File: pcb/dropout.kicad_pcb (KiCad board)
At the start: 2 copper layers, 228.6 x 94.4 mm, 62 parts, among them SW1 Rotary_Encoder_Switch, SW2 SW_Push, U1 ProMicro, U2 ProMicro

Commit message: alt-layout, replace encoder w/ switch
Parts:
- added K-FN1: MX-NoLED, MX_Only:MXOnly-1U-NoLED, F.Cu at (203.8, 59.5)
- SW1: moved to B.Cu
- moved C1 17.1 mm to (184.8, 65.6), turned to 270 degrees
- moved C2 15.4 mm to (188.0, 65.6), turned to 90 degrees
- moved SW1 4.80 mm to (196.2, 61.9)
- moved D15 1.53 mm to (197.3, 54.3)
- moved D10 0.47 mm to (192.0, 54.3)
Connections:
- SW1 pad S1: COL3 -> Net-(D15-Pad2)
- SW1 pad S2: Net-(D15-Pad2) -> COL3
- U1 pad 18: ROT-B -> ROT-A
- U1 pad 19: ROT-A -> ROT-B
- U2 pad 18: ROT-B -> ROT-A
- U2 pad 19: ROT-A -> ROT-B
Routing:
- net VCC: track 120.1 -> 101.0 mm
- net RESET: track 115.4 -> 96.7 mm
- net COL3: track 135.9 -> 145.7 mm, vias 0 -> 1
- net ROW0: track 74.4 -> 65.0 mm
- net ROT-A: track 42.7 -> 38.9 mm
- net ROT-B: track 43.8 -> 41.6 mm
- net Net-(D15-Pad2): track 13.1 -> 15.1 mm
- net GND: track 4.31 -> 5.72 mm, vias 1 -> 2

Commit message: 5v -> led -> pin (numlock led)
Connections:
- K-NUM1 pad 4: GND -> NUMLED
- R1 pad 2: NUMLED -> +5V
- U1 pad 24: (no net) -> +5V
- U2 pad 24: (no net) -> +5V
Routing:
- net +5V: track 0.00 -> 64.0 mm, vias 0 -> 3
- net NUMLED: track 49.9 -> 52.0 mm, vias 2 -> 1

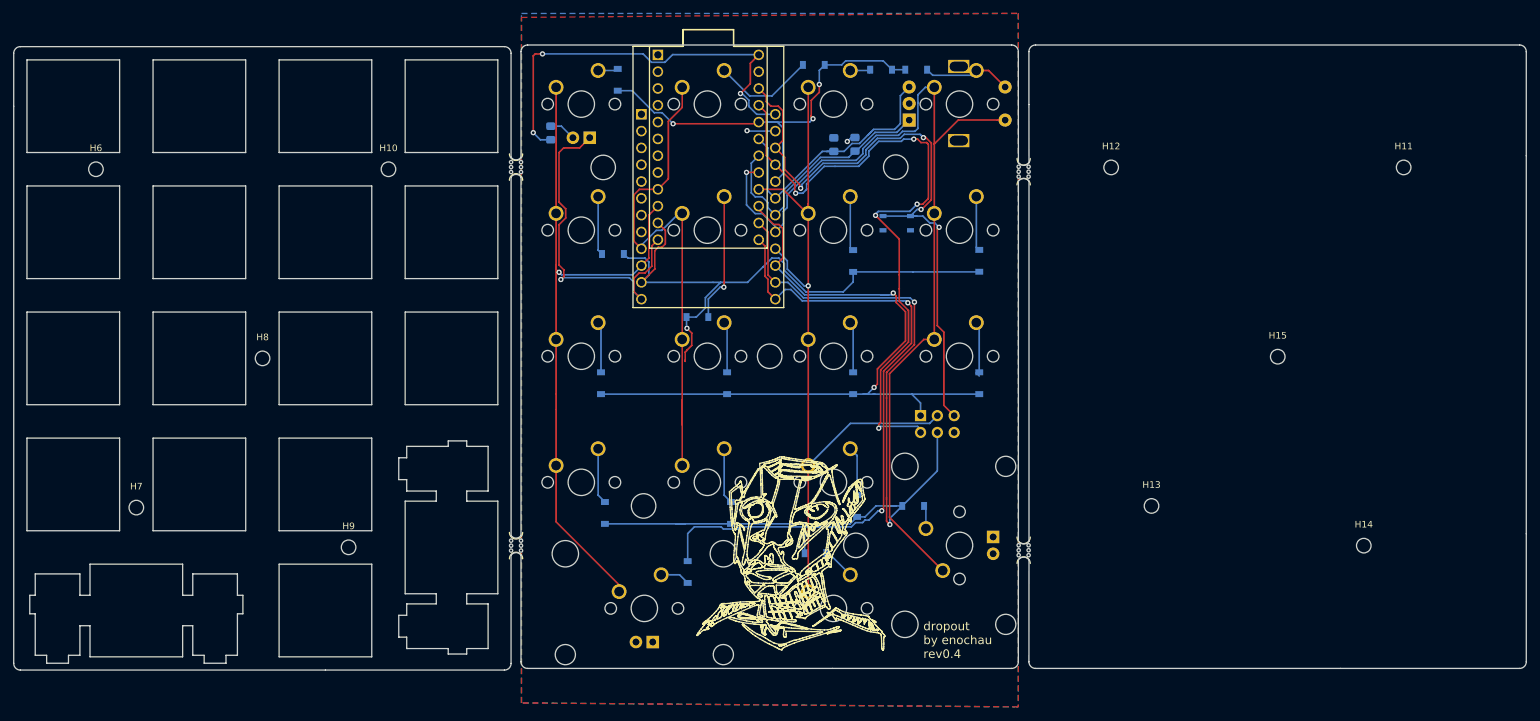
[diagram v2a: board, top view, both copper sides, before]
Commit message: i2c trrs connectors
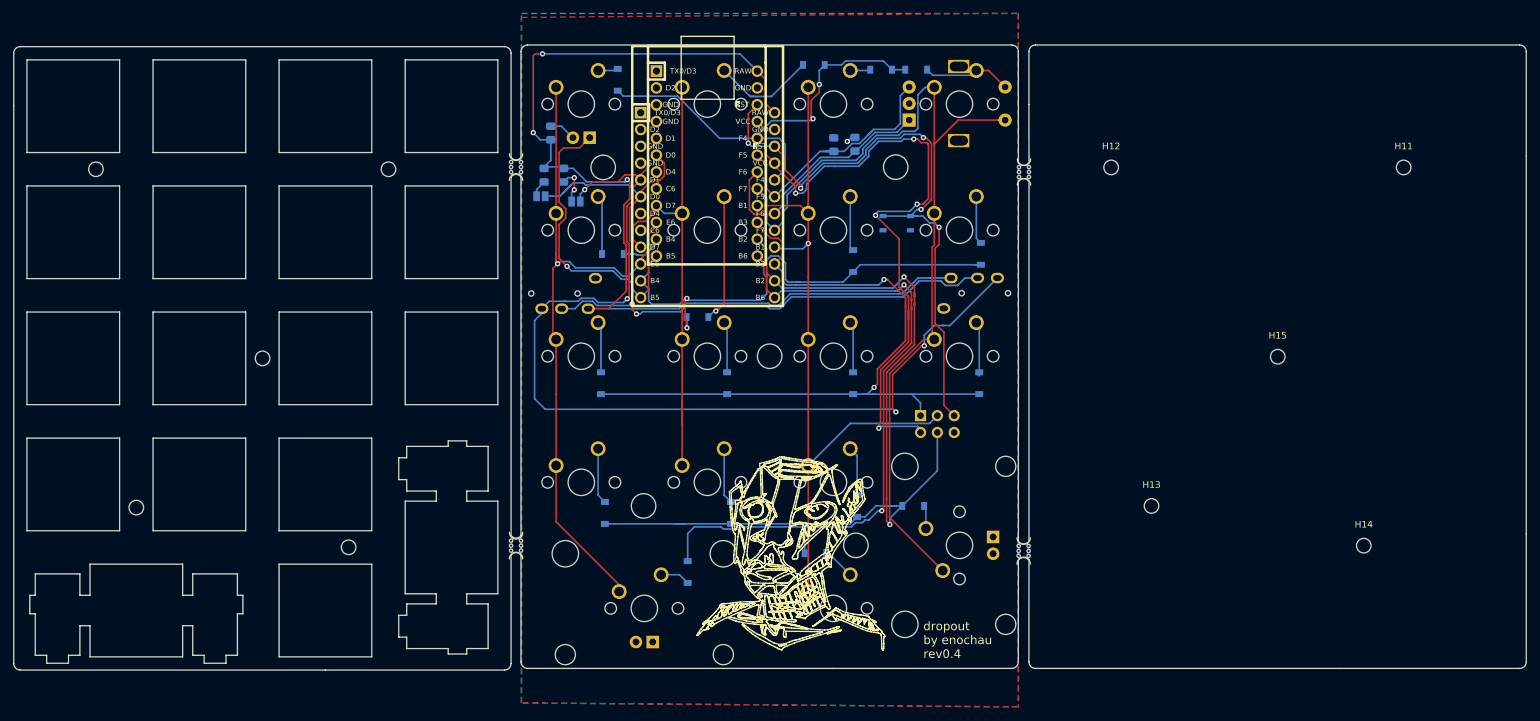
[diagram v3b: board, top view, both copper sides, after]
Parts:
- removed mouse-bite-2mm-slot (x4): VAL**, Panelization:mouse-bite-2mm-slot
- added H16: mouse-bites, Panelization:mouse-bite-2mm-slot, F.Cu at (136.8, 69.0)
- added H17: mouse-bites, Panelization:mouse-bite-2mm-slot, F.Cu at (213.6, 69.8)
- added H18: mouse-bites, Panelization:mouse-bite-2mm-slot, F.Cu at (213.5, 127.0)
- added H19: mouse-bites, Panelization:mouse-bite-2mm-slot, F.Cu at (136.8, 126.2)
- added J1: TRRS-conn, Keebio-Parts:TRRS-PJ-320A, B.Cu at (137.5, 88.1)
- added J2: TRRS-conn, Keebio-Parts:TRRS-PJ-320A, B.Cu at (212.7, 88.1)
- added JP1: Jumper, Jumper:SolderJumper-2_P1.3mm_Open_Pad1.0x1.5mm, B.Cu at (145.8, 74.2)
- added JP2: Jumper, Jumper:SolderJumper-2_P1.3mm_Open_Pad1.0x1.5mm, B.Cu at (140.6, 73.4)
- added R2: 4.7k, Resistor_SMD:R_0805_2012Metric_Pad1.15x1.40mm_HandSolder, B.Cu at (144.0, 70.2)
- added R3: 4.7k, Resistor_SMD:R_0805_2012Metric_Pad1.15x1.40mm_HandSolder, B.Cu at (141.0, 70.2)
- U1: footprint promicro:ProMicro_MiniUsb -> Keebio-Parts:ArduinoProMicro-Mini-USB
- U2: footprint promicro:ProMicro -> Keebio-Parts:ArduinoProMicro
- moved U2 2.47 mm to (165.6, 68.5)
- moved D16 1.08 mm to (207.0, 82.1)
- moved U1 0.27 mm to (165.8, 74.8)
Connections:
- U1 pad 5: (no net) -> SCL
- U1 pad 6: (no net) -> SDA
- U2 pad 5: (no net) -> SCL
- U2 pad 6: (no net) -> SDA
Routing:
- net SCL: track 0.00 -> 151.1 mm, vias 0 -> 4
- net SDA: track 0.00 -> 111.8 mm, vias 0 -> 2
- net +5V: track 64.0 -> 157.1 mm
- net ROW1: track 93.0 -> 85.4 mm, vias 1 -> 2
- net NUMLED: track 52.0 -> 44.9 mm
- net COL1: track 81.5 -> 74.8 mm
- net Net-(JP1-Pad1): track 0.00 -> 5.92 mm, vias 0 -> 2
- net COL3: track 145.7 -> 139.8 mm, vias 1 -> 0
- net GND: track 5.72 -> 1.41 mm, vias 2 -> 1
- net COL2: track 117.7 -> 114.0 mm
- net Net-(JP2-Pad1): track 0.00 -> 2.79 mm
- net ROW0: track 65.0 -> 66.7 mm, vias 3 -> 2
- net ROW3: track 133.4 -> 134.9 mm
- net ROT-A: track 38.9 -> 37.8 mm
- net VCC: track 101.0 -> 100.0 mm
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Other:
- board text removed: "RAW"
- board text removed: "TX0"

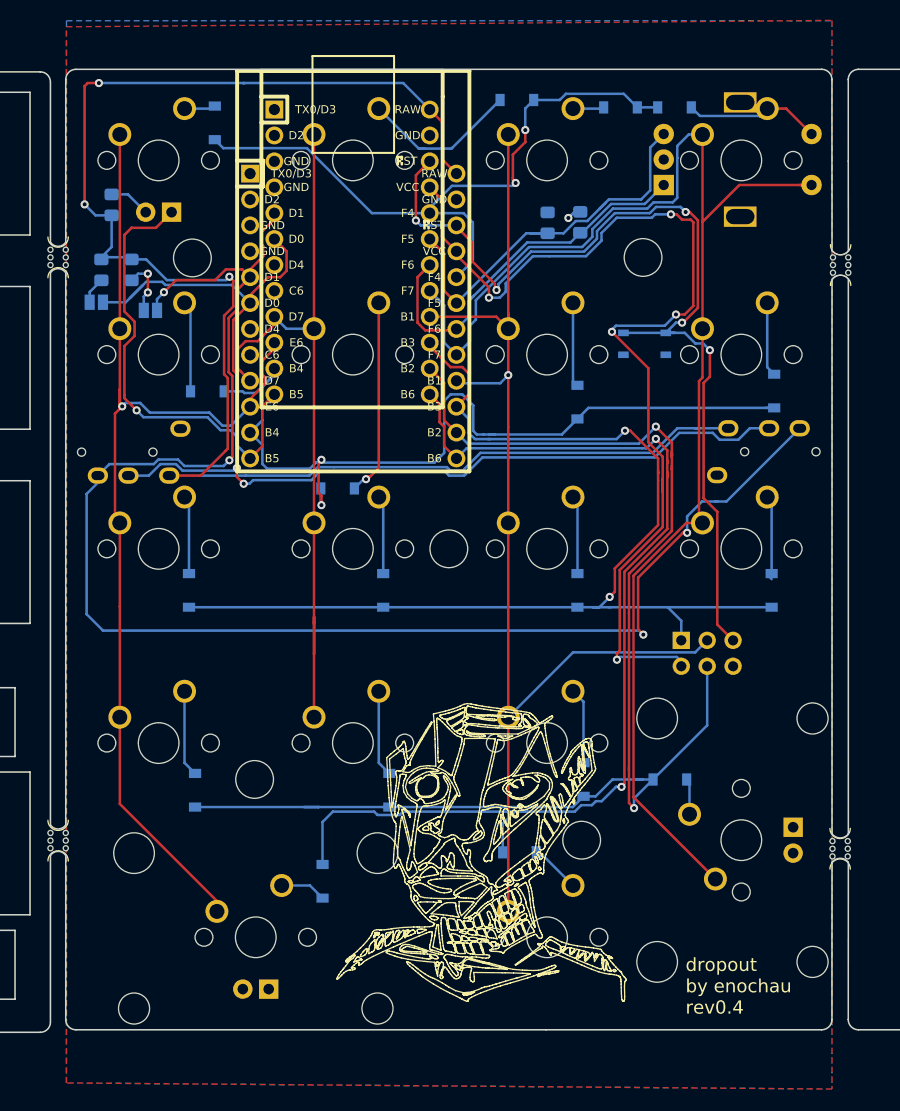
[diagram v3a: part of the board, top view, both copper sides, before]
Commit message: replace i2c trrs with header pins
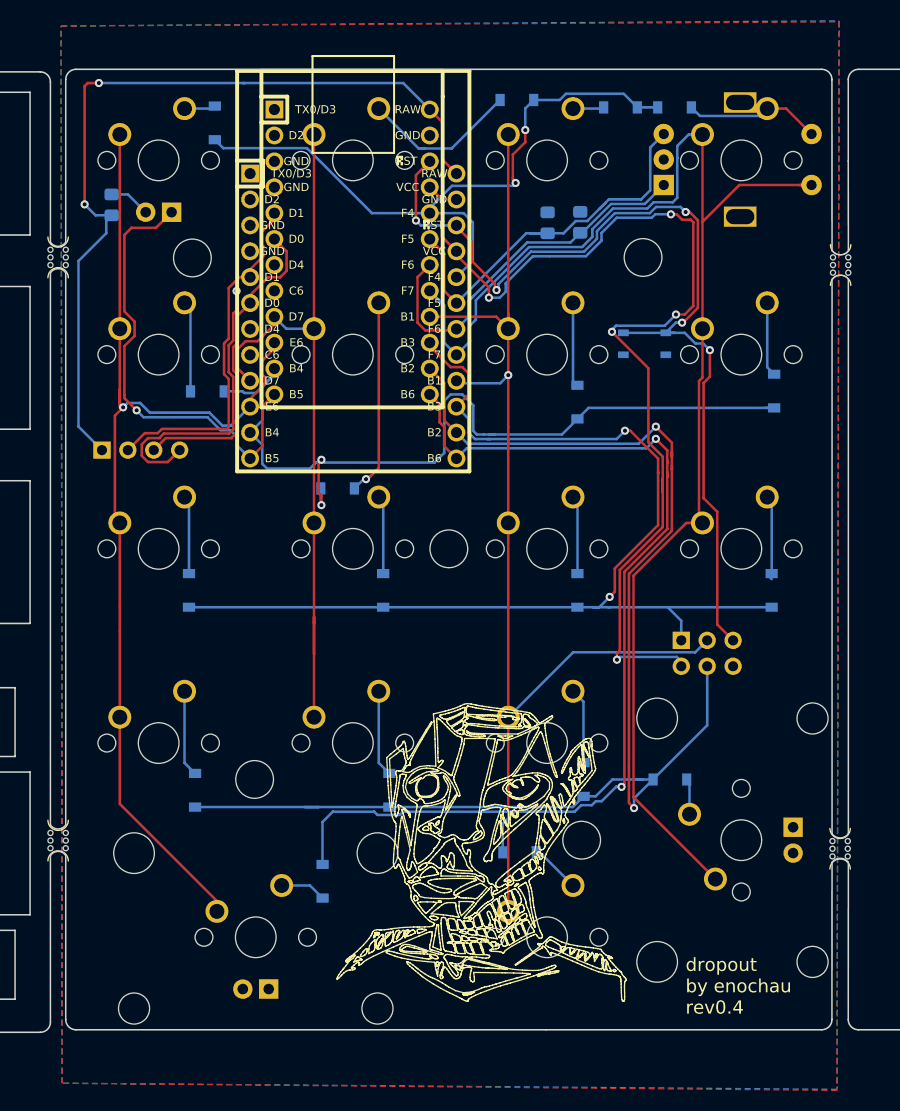
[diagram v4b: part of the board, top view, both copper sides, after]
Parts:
- removed J2: TRRS-conn, Keebio-Parts:TRRS-PJ-320A
- removed JP1, JP2: Jumper, Jumper:SolderJumper-2_P1.3mm_Open_Pad1.0x1.5mm
- removed R2, R3: 4.7k, Resistor_SMD:R_0805_2012Metric_Pad1.15x1.40mm_HandSolder
- J1: value TRRS-conn -> Conn_01x04_Male; footprint Keebio-Parts:TRRS-PJ-320A -> Connector_PinHeader_2.54mm:PinHeader_1x04_P2.54mm_Vertical
- moved J1 3.61 mm to (141.1, 87.9)
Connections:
- J1 pad 1: GND -> +5V
- J1 pad 2: +5V -> SCL
- J1 pad 4: SCL -> GND
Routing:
- net SCL: track 151.1 -> 35.2 mm, vias 4 -> 0
- net SDA: track 111.8 -> 31.4 mm, vias 2 -> 0
- net +5V: track 157.1 -> 82.9 mm, vias 3 -> 2
- net GND: track 1.41 -> 29.8 mm
- net Net-(JP1-Pad1): track 5.92 -> 0.00 mm, vias 2 -> 0
- net Net-(JP2-Pad1): track 2.79 -> 0.00 mm
- net COL0: track 104.4 -> 105.5 mm
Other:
- board text added: "5V+"
- board text added: "GND"
- board text added: "RESET"
- board text added: "SCL"
- board text added: "SDA"

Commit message: updating to rev0.5
updating to rev0.5
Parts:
- removed J-ISP1: Conn_02x03_Counter_Clockwise, Connector_PinHeader_2.54mm:PinHeader_2x03_P2.54mm_Vertical
- removed J1: Conn_01x04_Male, Connector_PinHeader_2.54mm:PinHeader_1x04_P2.54mm_Vertical
- removed U2: ProMicro, Keebio-Parts:ArduinoProMicro
- D1, D10, D11, D12, D13, D14, D15, D16, D17, D18, D2, D3, D4, D5, D6, D7, D8, D9: footprint Diode_SMD:D_SOD-123 -> footprint:Diode_TH_SOD123
- H16, H17, H18, H19: footprint Panelization:mouse-bite-2mm-slot -> Keebio-Parts:breakaway-mousebites
- K-0, K-ENT1: footprint MX_Only:MXOnly-2U-ReversedStabilizers -> MX_Only:MXOnly-2U-ReversedStabilizers-NoLED
- U1: footprint Keebio-Parts:ArduinoProMicro-Mini-USB -> promicro:ProMico_mini&micro
- moved D1 31.1 mm to (150.9, 86.9), turned to 180 degrees
- moved D2 25.0 mm to (150.9, 107.2)
- moved SW2 19.4 mm to (180.5, 63.9)
- moved D3 18.1 mm to (166.8, 107.2), turned to 180 degrees
- moved D6 17.0 mm to (188.9, 69.1)
- moved D13 16.4 mm to (178.4, 107.2), turned to 0 degrees
- moved D17 16.2 mm to (198.0, 88.0), turned to 0 degrees
- moved D12 16.1 mm to (179.1, 88.1), turned to 0 degrees
- moved D16 16.0 mm to (194.1, 91.4)
- moved D15 14.4 mm to (200.0, 68.5)
- moved D11 13.1 mm to (194.1, 94.7), turned to 270 degrees
- moved D18 12.9 mm to (196.5, 107.3)
- moved D9 12.5 mm to (175.0, 110.1), turned to 270 degrees
- moved D8 12.5 mm to (156.2, 102.5)
- moved D4 11.2 mm to (139.9, 125.5), turned to 270 degrees
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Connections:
- net RESET renamed Net-(SW2-Pad2)
- U1 pad 1: (no net) -> Net-(U1-Pad1)
- U1 pad 2: (no net) -> Net-(U1-Pad2)
- U1 pad 21: VCC -> Net-(U1-Pad21)
- U1 pad 5: SCL -> Net-(U1-Pad5)
- U1 pad 6: SDA -> Net-(U1-Pad6)
- U1 pad 7: (no net) -> Net-(U1-Pad7)
- U1 pad 8: (no net) -> Net-(U1-Pad8)
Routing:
- net VCC: track 100.0 -> 0.00 mm, vias 5 -> 0
- net ROW0: track 66.7 -> 158.8 mm, vias 2 -> 4
- net Net-(SW2-Pad2): track 95.9 -> 15.6 mm, vias 5 -> 0
- net ROW4: track 106.9 -> 68.1 mm, vias 2 -> 0
- net Net-(D1-Pad2): track 3.07 -> 40.6 mm, vias 0 -> 1
- net Net-(D2-Pad2): track 8.93 -> 44.7 mm, vias 0 -> 1
- net SCL: track 35.2 -> 0.00 mm
- net SDA: track 31.4 -> 0.00 mm
- net GND: track 29.8 -> 0.00 mm
- net Net-(D11-Pad2): track 8.37 -> 37.6 mm
- net ROW2: track 111.4 -> 86.9 mm, vias 2 -> 0
- net Net-(D18-Pad2): track 3.53 -> 26.8 mm, vias 0 -> 1
- net Net-(D4-Pad2): track 8.48 -> 29.6 mm, vias 0 -> 2
- net +5V: track 82.9 -> 62.7 mm, vias 2 -> 3
- net Net-(D16-Pad2): track 7.29 -> 23.8 mm, vias 0 -> 1
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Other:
- board size 228.6 x 94.4 mm -> 226.7 x 94.4 mm
- board text added: "dropout by enochau rev0.5"
- board text removed: "5V+"
- board text removed: "GND"
- board text removed: "RESET"
- board text removed: "SCL"
- board text removed: "SDA"
- board text removed: "VCC"
- board text removed: "dropout by enochau rev0.4"

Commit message: updating gerbers
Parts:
- moved H18 0.81 mm to (213.3, 126.2)
- moved H17 0.54 mm to (213.3, 69.1)
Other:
- outline, holes or cut-outs redrawn
